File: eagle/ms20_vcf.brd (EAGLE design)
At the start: 97.5 x 48.2 mm, 51 parts, among them IC1 LM13700N, IC2 TL082P, IC3 TL082P, Q1 2N3906, Q2 2N3906, U2 POWER

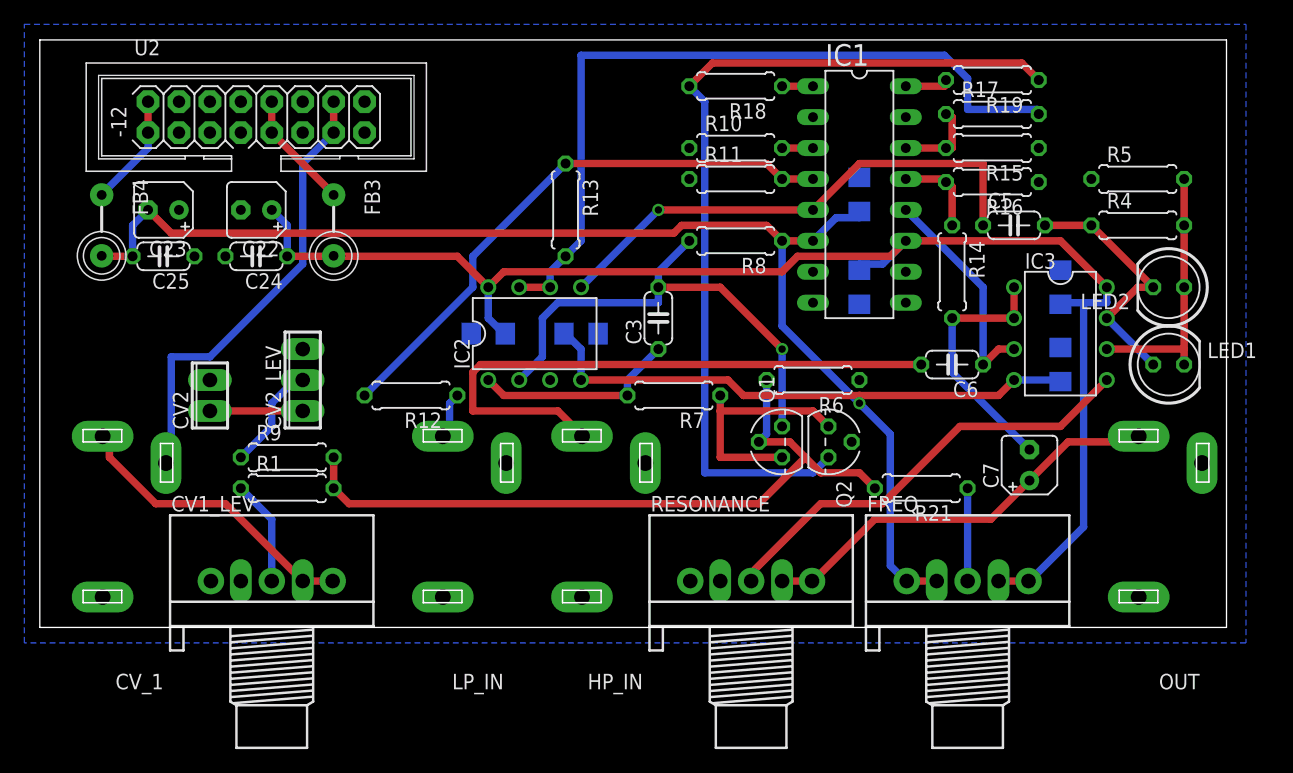
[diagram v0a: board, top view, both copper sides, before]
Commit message: labels adjusted for visibility
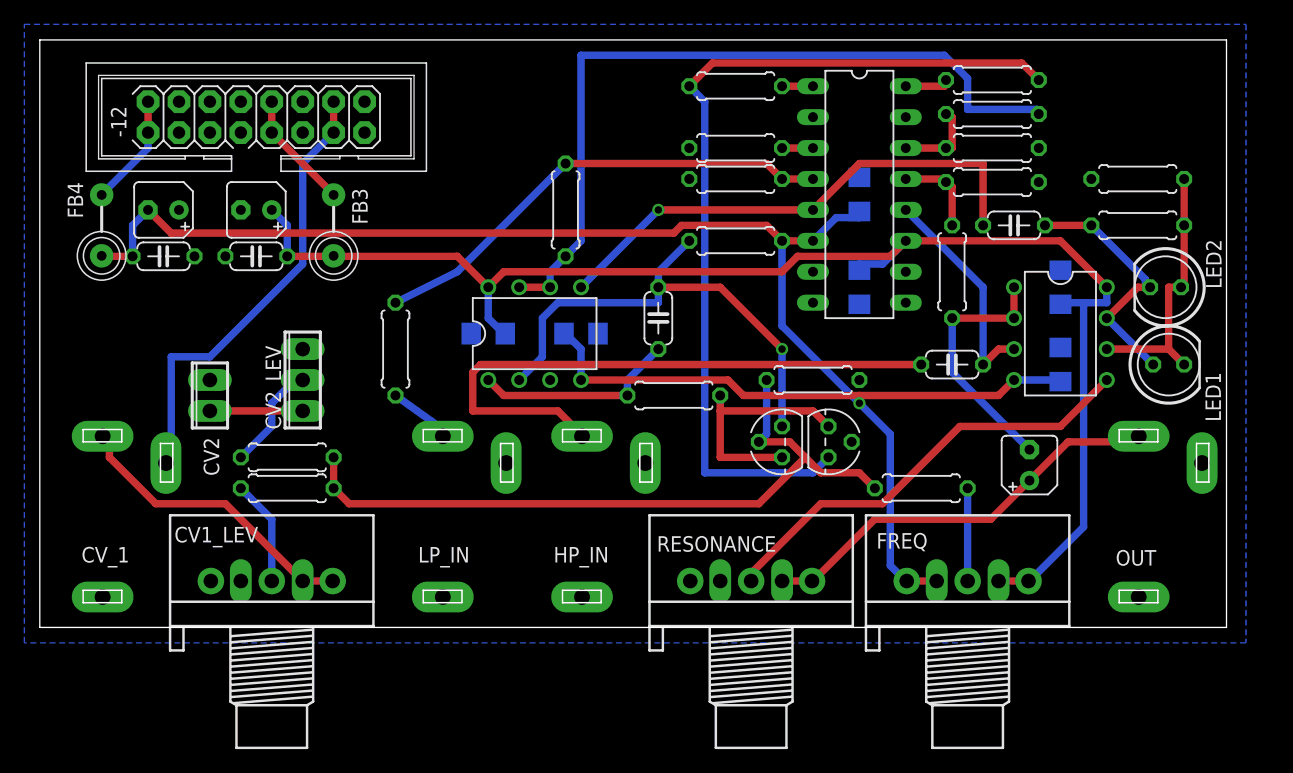
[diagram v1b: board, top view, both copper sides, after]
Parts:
- moved R12 4.02 mm to (29.2, 22.9), turned to 90 degrees
- moved LED2 0.25 mm to (92.5, 27.9)
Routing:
- net N$14: track 46.7 -> 39.1 mm
- net N$25: track 4.02 -> 6.04 mm
- net N$1: track 21.6 -> 22.1 mm

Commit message: reordered pots and jacks
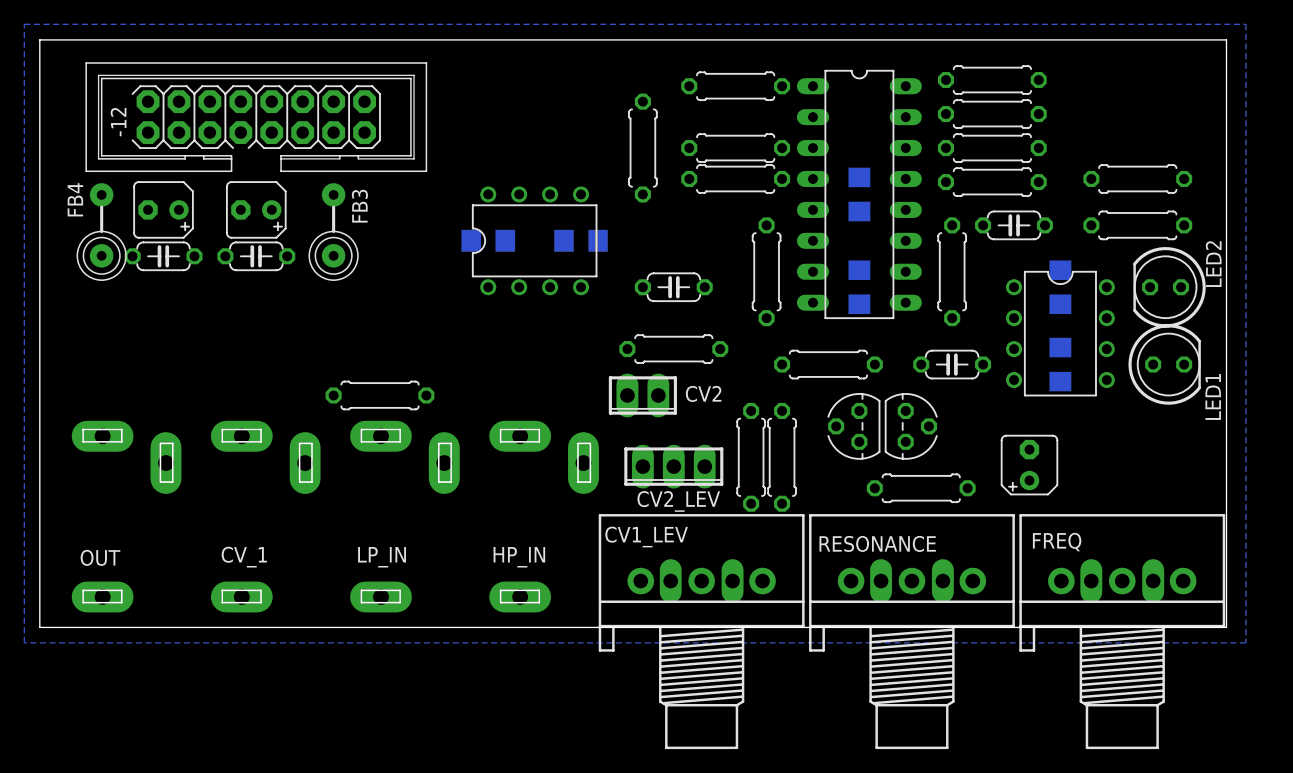
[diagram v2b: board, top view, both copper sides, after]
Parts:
- moved OUT 85.1 mm to (10.2, 0.00)
- moved R1 40.7 mm to (61.0, 14.0), turned to 90 degrees
- moved R9 38.1 mm to (58.4, 14.0), turned to 90 degrees
- moved CV2 35.6 mm to (49.5, 19.1), turned to 180 degrees
- moved CV1_LEV 35.3 mm to (54.4, 3.81)
- moved CV2_LEV 31.3 mm to (52.1, 13.2), turned to 180 degrees
- moved RESONANCE 13.2 mm to (71.6, 3.81)
- moved FREQ 12.7 mm to (88.9, 3.81)
- moved CV_1 11.4 mm to (21.6, 0.00)
- moved R13 8.13 mm to (49.5, 39.4)
- moved C4 7.62 mm to (36.8, 31.8)
- moved C8 7.62 mm to (44.5, 31.8)
- moved IC2 7.62 mm to (40.6, 31.8)
- moved Q2 6.48 mm to (71.1, 16.5)
- moved Q1 6.48 mm to (67.3, 16.5)
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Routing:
- net -12V: track 148.5 -> 0.00 mm, vias 1 -> 0
- net +12V: track 117.9 -> 0.00 mm
- net N$16: track 73.0 -> 0.00 mm
- net N$19: track 63.8 -> 0.00 mm
- net N$21: track 59.8 -> 0.00 mm
- net N$26: track 50.1 -> 0.00 mm
- net N$9: track 42.3 -> 0.00 mm, vias 1 -> 0
- net N$3: track 40.7 -> 0.00 mm, vias 1 -> 0
- net N$14: track 39.1 -> 0.00 mm
- net N$27: track 37.2 -> 0.00 mm
- net N$6: track 36.4 -> 0.00 mm
- net N$12: track 34.4 -> 0.00 mm
- net N$24: track 24.5 -> 0.00 mm
- net N$1: track 22.1 -> 0.00 mm
- net N$2: track 21.1 -> 0.00 mm
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
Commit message: slightly shallower
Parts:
- moved C4 6.84 mm to (39.4, 25.4), turned to 270 degrees
- moved C8 5.24 mm to (39.4, 33.0), turned to 270 degrees
- moved IC2 2.84 mm to (39.4, 29.2), turned to 90 degrees
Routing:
- net -12V: track 0.00 -> 151.9 mm
- net +12V: track 0.00 -> 107.9 mm
- net N$12: track 0.00 -> 95.4 mm
- net N$16: track 0.00 -> 66.3 mm
- net N$19: track 0.00 -> 66.3 mm
- net N$24: track 0.00 -> 52.1 mm
- net N$14: track 0.00 -> 51.4 mm
- net N$9: track 0.00 -> 50.9 mm
- net N$26: track 0.00 -> 35.9 mm
- net N$27: track 0.00 -> 32.2 mm
- net N$3: track 0.00 -> 30.9 mm
- net N$5: track 0.00 -> 29.9 mm
- net N$6: track 0.00 -> 25.8 mm
- net N$2: track 0.00 -> 22.3 mm
- net N$1: track 0.00 -> 22.1 mm
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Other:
- board size 97.5 x 48.2 mm -> 97.5 x 47.5 mm
